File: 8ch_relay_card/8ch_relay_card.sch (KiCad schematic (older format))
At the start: 19 parts

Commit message: More work on the schematic
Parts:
- added J? (x8): Conn_01x03, symbol Conn_01x03
- added RL1, RL? (x7): RM85-2011-35-1012, symbol RM85-2011-35-1012
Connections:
- net +12V: now also RL1.1 (+), RL?.1 (+), RL?.1 (+), RL?.1 (+), RL?.1 (+), RL?.1 (+), RL?.1 (+), RL?.1 (+)
- net OUT8: now reaches U?.11 (OUT8)
- net OUT7: now reaches U?.12 (OUT7)
- net OUT6: now reaches U?.13 (OUT6)
- net OUT5: now reaches U?.14 (OUT5)
- net OUT4: now reaches U?.15 (OUT4)
- net OUT3: now reaches U?.16 (OUT3)
- net OUT2: now reaches U?.17 (OUT2)
- net OUT1: now reaches U?.18 (OUT1)
- net OUT1: now also RL1.2 (-), RL?.2 (-), RL?.2 (-), RL?.2 (-), RL?.2 (-), RL?.2 (-), RL?.2 (-), RL?.2 (-)
- new net RL1_COM: J?.2 (Pin_2), J?.2 (Pin_2), J?.2 (Pin_2), J?.2 (Pin_2), J?.2 (Pin_2), J?.2 (Pin_2), J?.2 (Pin_2), J?.2 (Pin_2), RL1.4, RL1.7, RL?.4, RL?.4, RL?.4, RL?.4, RL?.4, RL?.4, RL?.4, RL?.7, RL?.7, RL?.7, RL?.7, RL?.7, RL?.7, RL?.7
- new net RL1_NC: J?.1 (Pin_1), J?.1 (Pin_1), J?.1 (Pin_1), J?.1 (Pin_1), J?.1 (Pin_1), J?.1 (Pin_1), J?.1 (Pin_1), J?.1 (Pin_1), RL1.3, RL1.6, RL?.3, RL?.3, RL?.3, RL?.3, RL?.3, RL?.3, RL?.3, RL?.6, RL?.6, RL?.6, RL?.6, RL?.6, RL?.6, RL?.6
- new net RL1_NO: J?.3 (Pin_3), J?.3 (Pin_3), J?.3 (Pin_3), J?.3 (Pin_3), J?.3 (Pin_3), J?.3 (Pin_3), J?.3 (Pin_3), J?.3 (Pin_3), RL1.5, RL1.8, RL?.5, RL?.5, RL?.5, RL?.5, RL?.5, RL?.5, RL?.5, RL?.8, RL?.8, RL?.8, RL?.8, RL?.8, RL?.8, RL?.8
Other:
- note added: "Switchable Pull-ups:\n\nSelect:\n\n* No pull\n* Pull GND\n* Pull 12V\n* Pull V IO (e.g. voltage \n from attached DIO box)"
- note removed: "Switchable Pull-ups:\n\nSelect:\n\n* No pull\n* Pull GND\n* Pull 12V\n* Pull V IO (e.g. voltage from attached DIO box)"
- moved on the sheet: J?, P?, R?, U?A

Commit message: First revision of schematic completed
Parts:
- added C1: 100n, symbol C
- added C2: 100u, symbol CP1
- added D1, D2, D3, D4, D5, D6, D7, D8: L-59EGW, symbol LED_Dual_ACA
- added D10: BZT55C12, symbol D_Zener
- added D9: LED, symbol LED
- added J19: jmp_2way, symbol jmp_2way
- added J20: TruConnect 21-3000, symbol Conn_01x02
- added Q1, Q10, Q11, Q12, Q13, Q14, Q15, Q16, Q2, Q3, Q4, Q5, Q6, Q7, Q8, Q9: 2N7002, TO_SOT_Packages_SMD:SOT-23, symbol 2N7002
- added Q17: STD12NF06L, symbol Q_NMOS_GDS
- added R10, R11, R12, R21, R22, R23, R24, R34, R9: 10k, symbol R
- added R13, R14, R15, R16, R17, R18, R19, R20, R25, R26, R27, R28, R29, R30, R31, R32, R33: 470, symbol R
- added unit 2 of U1
- J1: renamed from P?; value CONN_01X10 -> DIGITAL INPUT
- J11, J12, J13, J14, J15, J16, J17, J18: renamed from J?; value Conn_01x03 -> TruConnect XY-305
- gave numbers to parts that had none: 25
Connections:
- net labels added: +12V_SW_BJH, RL2_COM, RL2_NC, RL2_NO, RL3_COM, RL3_NC, RL3_NO, RL4_COM, RL4_NC, RL4_NO, RL5_COM, RL5_NC, RL5_NO, RL6_COM, RL6_NC, RL6_NO, RL7_COM, RL7_NC, RL7_NO, RL8_COM, RL8_NC, RL8_NO
- wire segments 189 -> 359
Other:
- note added: "12V_SW\nSelect:\nOutput Display ON/OFF"
- note added: "INDICATION"
- note added: "INPUT RELAY\nDRIVER"
- note added: "POWER"
- note added: "RELAYS"
- moved on the sheet: J1, J10, J15, J16, J17, J18, J2, J3, J4, J5, J6, J7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

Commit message: scheamtic finished, PCB almost done
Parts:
- C1: footprint (none) -> Capacitors_SMD:C_0805_HandSoldering
- C2: footprint (none) -> Capacitors_SMD:c_elec_8x10.5
- D1, D2, D3, D4, D5, D6, D7, D8: footprint (none) -> LEDs:LED-5MM-3
- D10: footprint (none) -> bjh-kicad-rcld-fp:BZT55
- D9: footprint (none) -> LEDs:LED-5MM
- J1: value DIGITAL INPUT -> CamdenBoss CTB3051/10BK; footprint (none) -> bjh-kicad-connector-fp:CamdenBossCTB3051_10BK
- J10, J2, J3, J4, J5, J6, J7, J8, J9: footprint (none) -> bjh-kicad-connector-fp:HEAD-1row-2.54mm-3way
- J11, J12, J13, J14, J15, J16, J17, J18: footprint (none) -> bjh-kicad-connector-fp:TruConnect_21-1812
- J19: footprint (none) -> bjh-kicad-connector-fp:HEAD-1row-2.54mm-2way
- J20: footprint (none) -> bjh-kicad-connector-fp:TruConnect_21-3000
- Q17: footprint (none) -> bjh-kicad-transistor-fp:DPAK_DGS
- R1, R10, R11, R12, R13, R14, R15, R16, R17, R18, R19, R2, R20, R21, R22, R23, R24, R25, R26, R27, R28, R29, R3, R30, R31, R32, R33, R34, R4, R5, R6, R7, R8, R9: footprint (none) -> Resistors_SMD:R_0805
- RL1, RL2, RL3, RL4, RL5, RL6, RL7, RL8: footprint (none) -> bjh-kicad-relays:RM85-2011-35-1012
- U1: footprint (none) -> Housings_DIP:DIP-18_W7.62mm
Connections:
- wire segments 359 -> 360
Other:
- moved on the sheet: C1, C2, D1, D10, D2, D3, D4, D5, D6, D7, D8, D9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

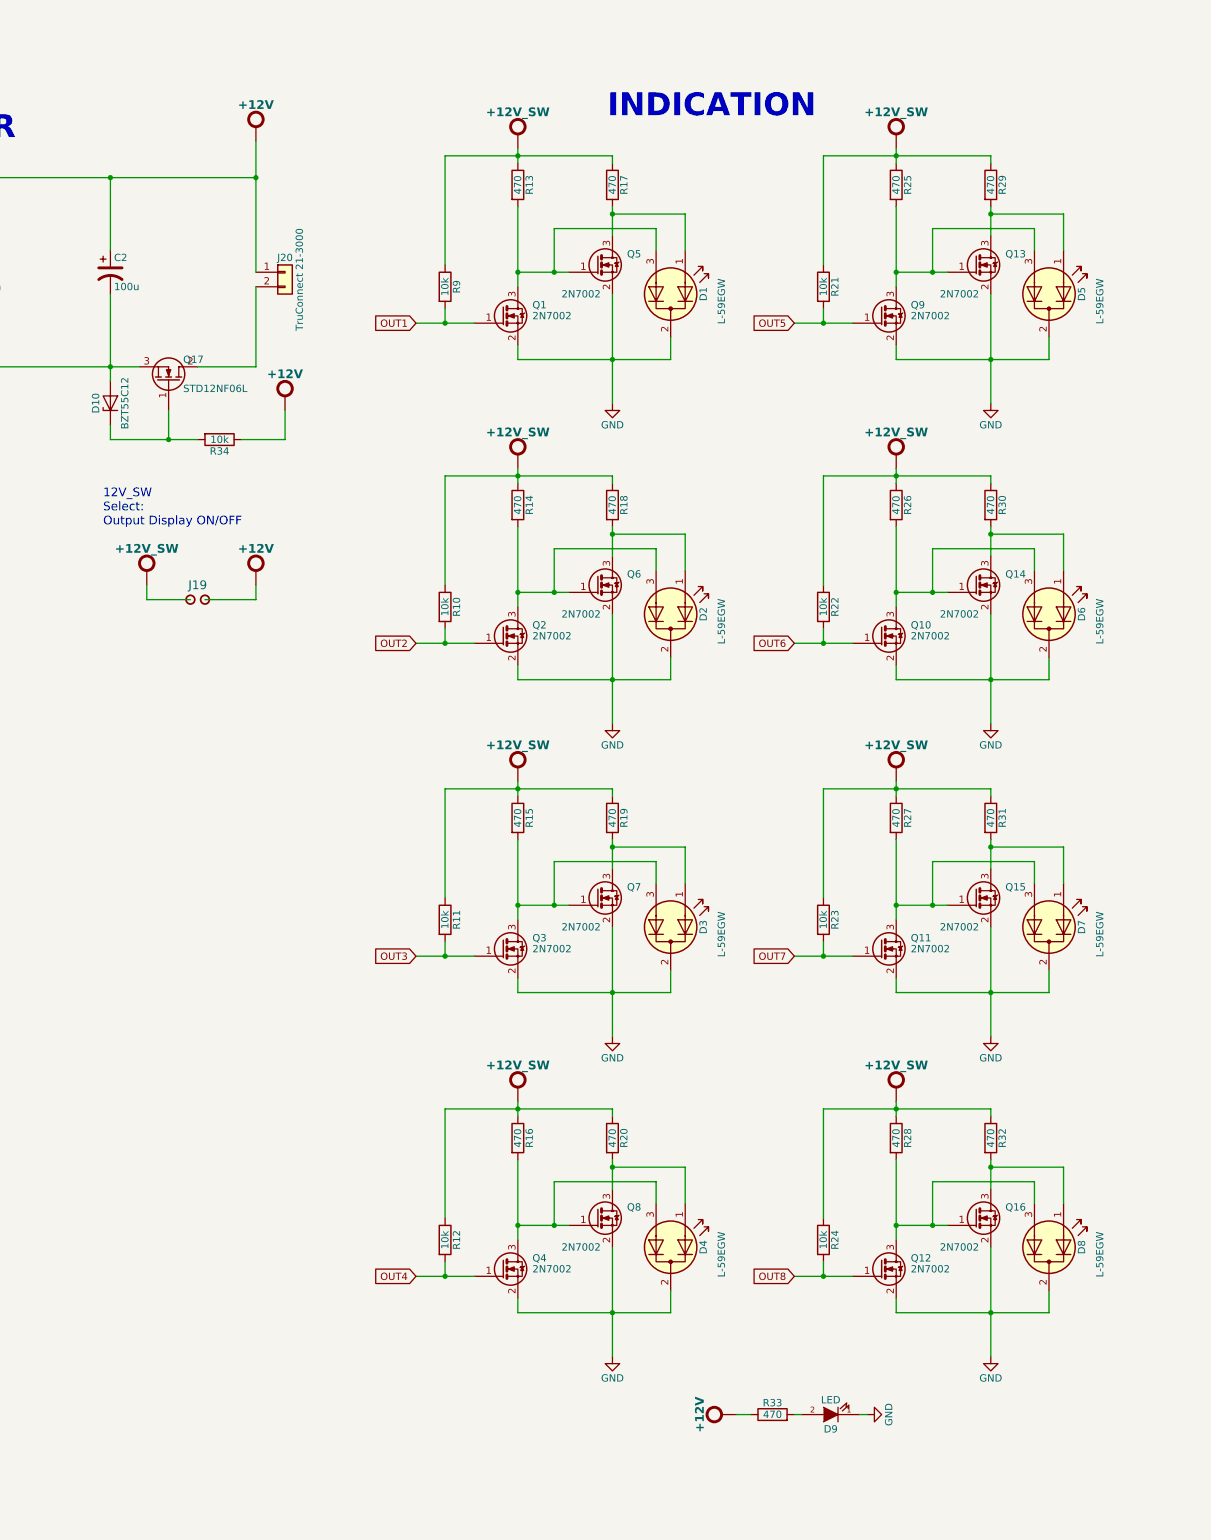
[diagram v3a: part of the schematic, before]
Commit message: Removed bi-colour LEDs and reverted to single colour LEDs.  PCB Design finished.
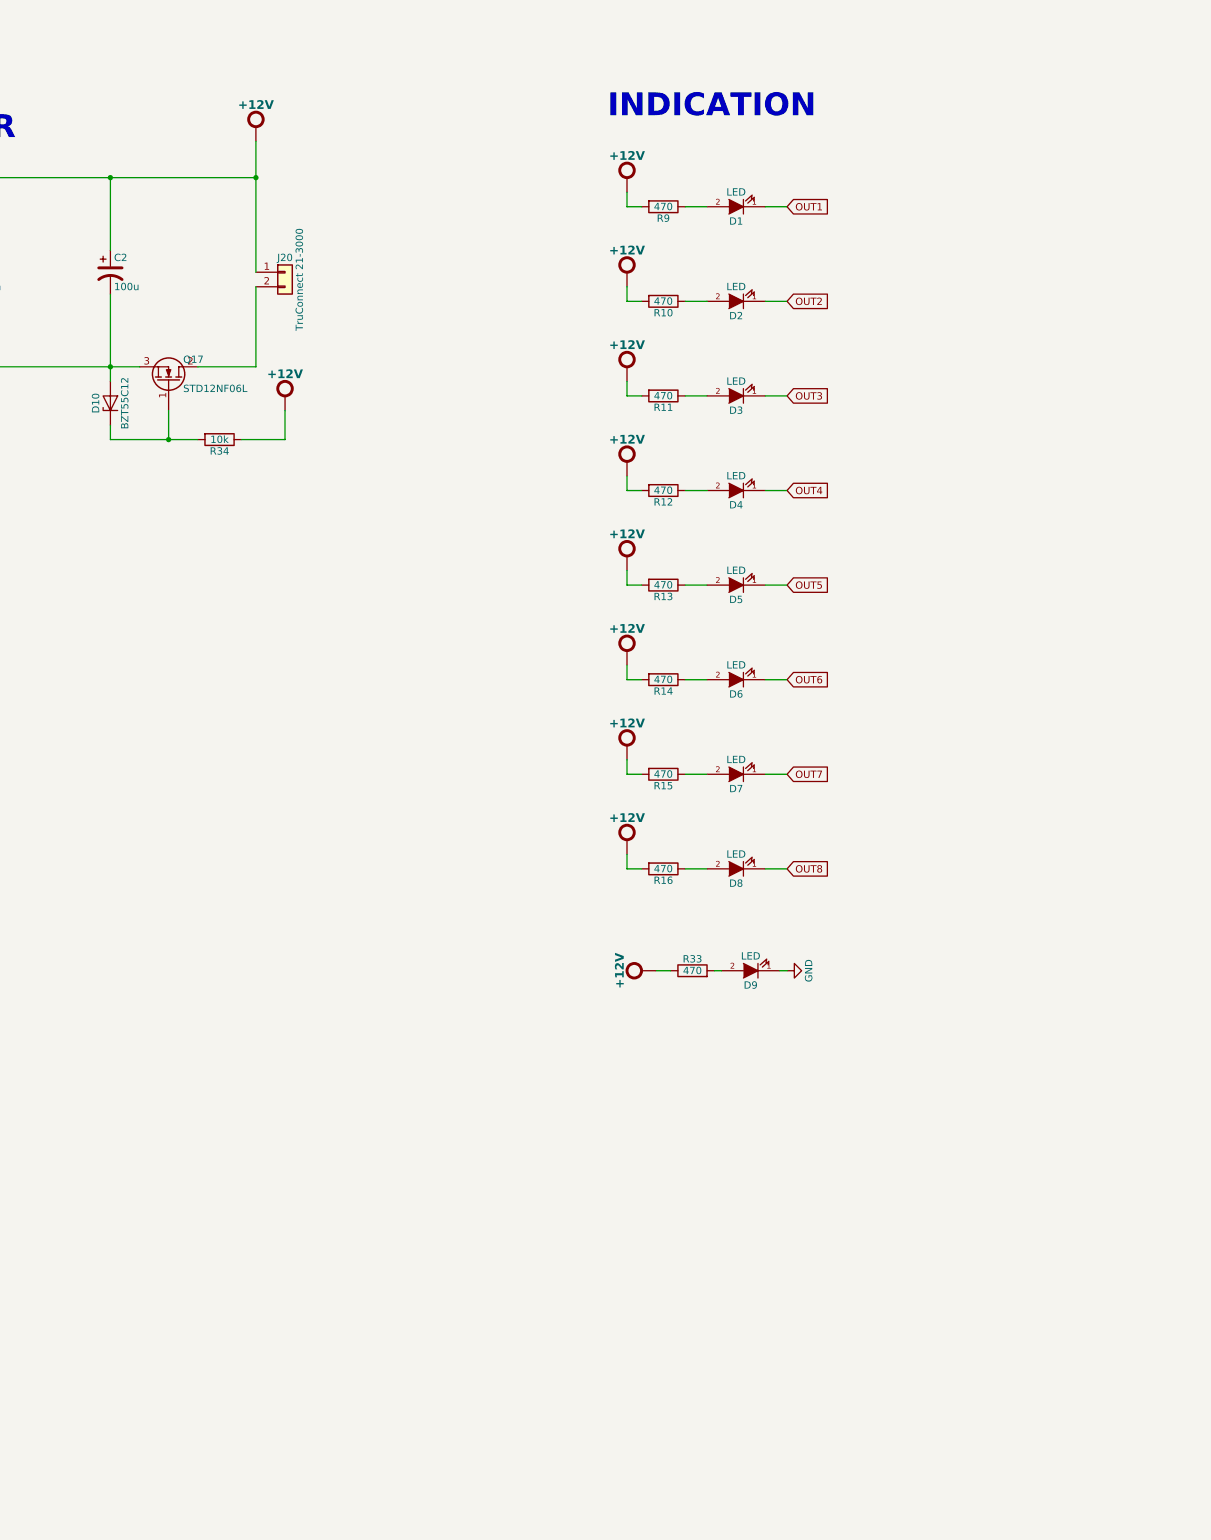
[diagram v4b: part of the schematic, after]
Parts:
- removed D1, D2, D3, D4, D5, D6, D7, D8: L-59EGW, LEDs:LED-5MM-3, symbol LED_Dual_ACA
- removed J19: jmp_2way, bjh-kicad-connector-fp:HEAD-1row-2.54mm-2way, symbol jmp_2way
- removed Q1, Q10, Q11, Q12, Q13, Q14, Q15, Q16, Q2, Q3, Q4, Q5, Q6, Q7, Q8, Q9: 2N7002, TO_SOT_Packages_SMD:SOT-23, symbol 2N7002
- removed R17, R18, R19, R20, R25, R26, R27, R28, R29, R30, R31, R32: 470, Resistors_SMD:R_0805, symbol R
- removed R21, R22, R23, R24: 10k, Resistors_SMD:R_0805, symbol R
- added D1, D2, D3, D4, D5, D6, D7, D8: LED, LEDs:LED-5MM, symbol LED
- R10, R11, R12, R9: value 10k -> 470
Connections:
- net +12V: now also R10.2, R11.2, R12.2, R13.2, R14.2, R15.2, R16.2, R9.2
- net +12V_SW: no longer R10.1, R11.1, R12.1, R13.1, R14.1, R15.1, R16.1, R9.1
- net OUT1: now also D1.1 (K); no longer R9.2
- net OUT2: now also D2.1 (K); no longer R10.2
- net OUT3: now also D3.1 (K); no longer R11.2
- net OUT4: now also D4.1 (K); no longer R12.2
- net OUT5: now also D5.1 (K)
- net OUT6: now also D6.1 (K)
- net OUT7: now also D7.1 (K)
- net OUT8: now also D8.1 (K)
- new net: D1.2 (A), R9.1
- new net: D2.2 (A), R10.1
- new net: D3.2 (A), R11.1
- new net: D4.2 (A), R12.1
- new net: D5.2 (A), R13.1
- new net: D6.2 (A), R14.1
- new net: D7.2 (A), R15.1
- new net: D8.2 (A), R16.1
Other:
- note removed: "12V_SW\nSelect:\nOutput Display ON/OFF"
- moved on the sheet: D9, R33
